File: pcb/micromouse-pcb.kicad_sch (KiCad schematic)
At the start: 40 parts, among them J1_MotorEncoder1 Conn_01x06, J2_MotorEncoder1 Conn_01x06, J3 Conn_01x08, J4 Conn_01x08, Q1 BS170, Q2 TEFT4300, Q3 BS170, Q4 TEFT4300, Q5 BS170, Q6 TEFT4300, Q7 BS170, Q8 TEFT4300, SW1 SW_SPDT, U0 Teensy 4.1, U1 L7805

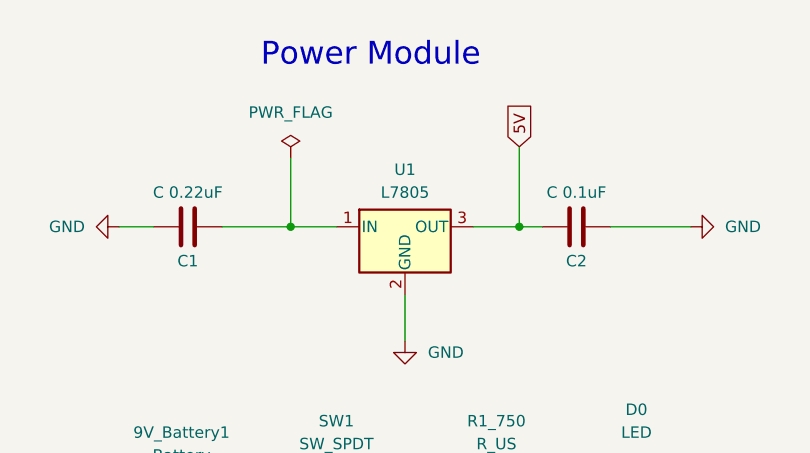
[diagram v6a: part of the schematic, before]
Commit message: !assigned random footprints, should be revised
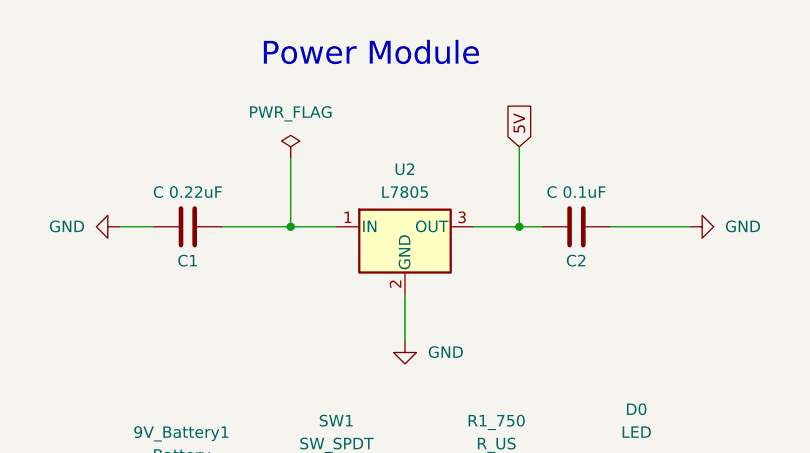
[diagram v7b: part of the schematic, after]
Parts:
- removed U1: L7805, symbol Regulator_Linear:L7805
- added U2: L7805, Package_TO_SOT_SMD:TO-252-3_TabPin2, symbol Regulator_Linear:L7805
- 9V_Battery1: footprint (none) -> Battery:BatteryHolder_MPD_BC12AAPC_2xAA
- D0: footprint (none) -> LED_THT:LED_D5.0mm_Clear
- J1_MotorEncoder1, J2_MotorEncoder1: footprint (none) -> Connector_PinHeader_2.54mm:PinHeader_1x06_P2.54mm_Horizontal
- J3, J4: footprint (none) -> Connector_PinHeader_2.54mm:PinHeader_1x08_P2.54mm_Horizontal
- SW1: footprint (none) -> Button_Switch_SMD:SW_SPDT_CK_JS102011SAQN
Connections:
- net 5V: now also U2.3 (OUT)
- net GND: now also U2.2 (GND)
- net at C1.1: now also U2.1 (IN)
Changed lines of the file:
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@@
 			)
 		)
-		(property "Footprint" ""
+		(property "Footprint" "LED_THT:LED_D5.0mm_Clear"
 			(at 370.84 74.93 0)
 			(effects
@@
 			)
 		)
-		(property "Footprint" ""
+		(property "Footprint" "Button_Switch_SMD:SW_SPDT_CK_JS102011SAQN"
 			(at 339.09 77.47 0)
 			(effects
@@
 			)
 		)
-		(property "Footprint" ""
+		(property "Footprint" "Connector_PinHeader_2.54mm:PinHeader_1x06_P2.54mm_Horizontal"
 			(at 240.03 44.45 0)
 			(effects
@@
 	)
 	(symbol
-		(lib_id "Regulator_Linear:L7805")
-		(at 346.71 46.99 0)
-		(unit 1)
-		(exclude_from_sim no)
-		(in_bom yes)
-		(on_board yes)
-		(dnp no)
-		(fields_autoplaced yes)
-		(property "Reference" "U1"
-			(at 346.71 40.64 0)
-			(effects
-				(font
-					(size 1.27 1.27)
-				)
-			)
-		)
-		(property "Value" "L7805"
-			(at 346.71 43.18 0)
-			(effects
-				(font
-					(size 1.27 1.27)
-				)
-			)
-		)
-		(property "Footprint" ""
-			(at 347.345 50.8 0)
-			(effects
-				(font
-					(size 1.27 1.27)
-					(italic yes)
-				)
-				(justify left)
-				(hide yes)
-			)
-		)
-		(property "Datasheet" "http://www.st.com/content/ccc/resource/technical/document/datasheet/41/4f/b3/b0/12/d4/47/88/CD00000444.pdf/files/CD00000444.pdf/jcr:content/translations/en.CD00000444.pdf"
-			(at 346.71 48.26 0)
-			(effects
-				(font
-					(size 1.27 1.27)
-				)
-				(hide yes)
-			)
-		)
-		(property "Description" "Positive 1.5A 35V Linear Regulator, Fixed Output 5V, TO-220/TO-263/TO-252"
-			(at 346.71 46.99 0)
-			(effects
-				(font
-					(size 1.27 1.27)
-				)
-				(hide yes)
-			)
-		)
-		(pin "1"
-		)
-		(pin "3"
-		)
-		(pin "2"
-		)
-		(instances
-			(project ""
-				(path "/6bab3514-b9e6-4652-bd2e-edc57bdbde3d"
-					(reference "U1")
-					(unit 1)
-				)
-			)
-		)
-	)
-	(symbol
 		(lib_id "power:GND")
 		(at 256.54 76.2 270)
@@
 			)
 		)
-		(property "Footprint" ""
+		(property "Footprint" "Battery:BatteryHolder_MPD_BC12AAPC_2xAA"
 			(at 322.834 77.47 90)
 			(effects
@@
 			)
 		)
-		(property "Footprint" ""
+		(property "Footprint" "Connector_PinHeader_2.54mm:PinHeader_1x06_P2.54mm_Horizontal"
 			(at 280.67 44.45 0)
 			(effects
@@
 	)
 	(symbol
+		(lib_id "Regulator_Linear:L7805")
+		(at 346.71 46.99 0)
+		(unit 1)
+		(exclude_from_sim no)
+		(in_bom yes)
+		(on_board yes)
+		(dnp no)
+		(fields_autoplaced yes)
+		(property "Reference" "U2"
+			(at 346.71 40.64 0)
+			(effects
+				(font
+					(size 1.27 1.27)
+				)
+			)
+		)
+		(property "Value" "L7805"
+			(at 346.71 43.18 0)
+			(effects
+				(font
+					(size 1.27 1.27)
+				)
+			)
+		)
+		(property "Footprint" "Package_TO_SOT_SMD:TO-252-3_TabPin2"
+			(at 347.345 50.8 0)
+			(effects
+				(font
+					(size 1.27 1.27)
+					(italic yes)
+				)
+				(justify left)
+				(hide yes)
+			)
+		)
+		(property "Datasheet" "http://www.st.com/content/ccc/resource/technical/document/datasheet/41/4f/b3/b0/12/d4/47/88/CD00000444.pdf/files/CD00000444.pdf/jcr:content/translations/en.CD00000444.pdf"
+			(at 346.71 48.26 0)
+			(effects
+				(font
+					(size 1.27 1.27)
+				)
+				(hide yes)
+			)
+		)
+		(property "Description" "Positive 1.5A 35V Linear Regulator, Fixed Output 5V, TO-220/TO-263/TO-252"
+			(at 346.71 46.99 0)
+			(effects
+				(font
+					(size 1.27 1.27)
+				)
+				(hide yes)
+			)
+		)
+		(pin "1"
+		)
+		(pin "3"
+		)
+		(pin "2"
+		)
+		(instances
+			(project ""
+				(path "/6bab3514-b9e6-4652-bd2e-edc57bdbde3d"
+					(reference "U2")
+					(unit 1)
+				)
+			)
+		)
+	)
+	(symbol
 		(lib_id "Transistor_FET:BS170")
 		(at 361.95 120.65 90)
@@
 			)
 		)
-		(property "Footprint" ""
+		(property "Footprint" "Connector_PinHeader_2.54mm:PinHeader_1x08_P2.54mm_Horizontal"
 			(at 261.62 78.74 0)
 			(effects
@@
 			)
 		)
-		(property "Footprint" ""
+		(property "Footprint" "Connector_PinHeader_2.54mm:PinHeader_1x08_P2.54mm_Horizontal"
 			(at 232.41 78.74 0)
 			(effects

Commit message: basically done, changed a few footprints
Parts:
- 7.4_LiPo1: renamed from 9V_Battery1; footprint Battery:BatteryHolder_MPD_BC12AAPC_2xAA -> Connector_PinHeader_2.54mm:PinHeader_1x02_P2.54mm_Vertical
- C1, C2: footprint Capacitor_SMD:C_0805_2012Metric_Pad1.18x1.45mm_HandSolder -> Capacitor_SMD:C_1206_3216Metric_Pad1.33x1.80mm_HandSolder
- J1_MotorEncoder1, J2_MotorEncoder1: footprint Connector_PinHeader_2.54mm:PinHeader_1x06_P2.54mm_Horizontal -> Connector_PinHeader_2.54mm:PinHeader_1x06_P2.54mm_Vertical
- J3, J4: footprint Connector_PinHeader_2.54mm:PinHeader_1x08_P2.54mm_Horizontal -> Connector_PinHeader_2.54mm:PinHeader_1x08_P2.54mm_Vertical
- R10, R11, R12, R13, R14, R15, R16, R17, R1_750, R2, R3, R4, R5, R6, R7, R8, R9: footprint Resistor_SMD:R_0805_2012Metric_Pad1.20x1.40mm_HandSolder -> Resistor_SMD:R_1206_3216Metric_Pad1.30x1.75mm_HandSolder
- SW1: footprint Button_Switch_SMD:SW_SPDT_CK_JS102011SAQN -> Connector_PinHeader_2.54mm:PinHeader_1x03_P2.54mm_Vertical
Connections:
- net +9V is gone; now on net 7.4V: D0.1 (K)
- net 7.4V: now reaches C1.1, U2.1 (IN)
